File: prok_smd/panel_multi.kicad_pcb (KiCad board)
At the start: 2 copper layers, 80 x 128.5 mm, 4 parts

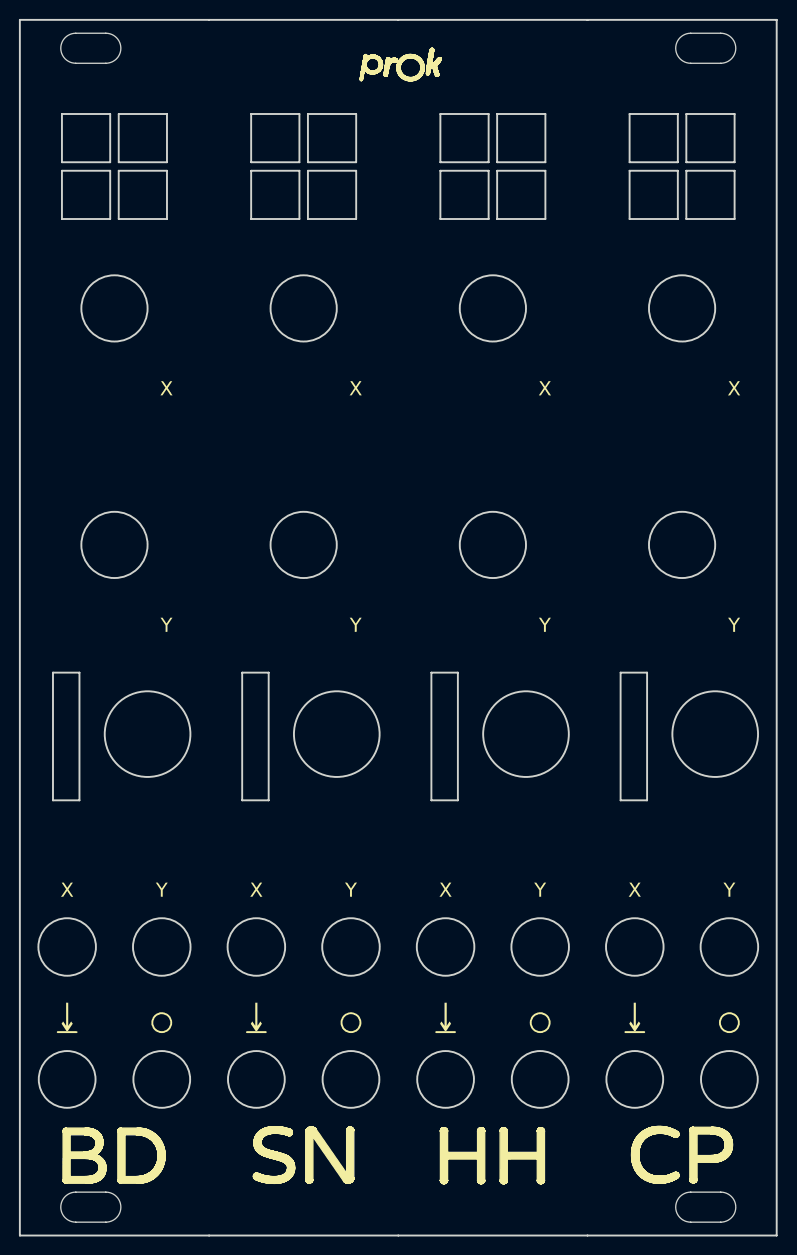
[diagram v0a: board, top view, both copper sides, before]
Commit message: :lipstick: Panel (x4) changed graphics (plaits style) & changed name ;)
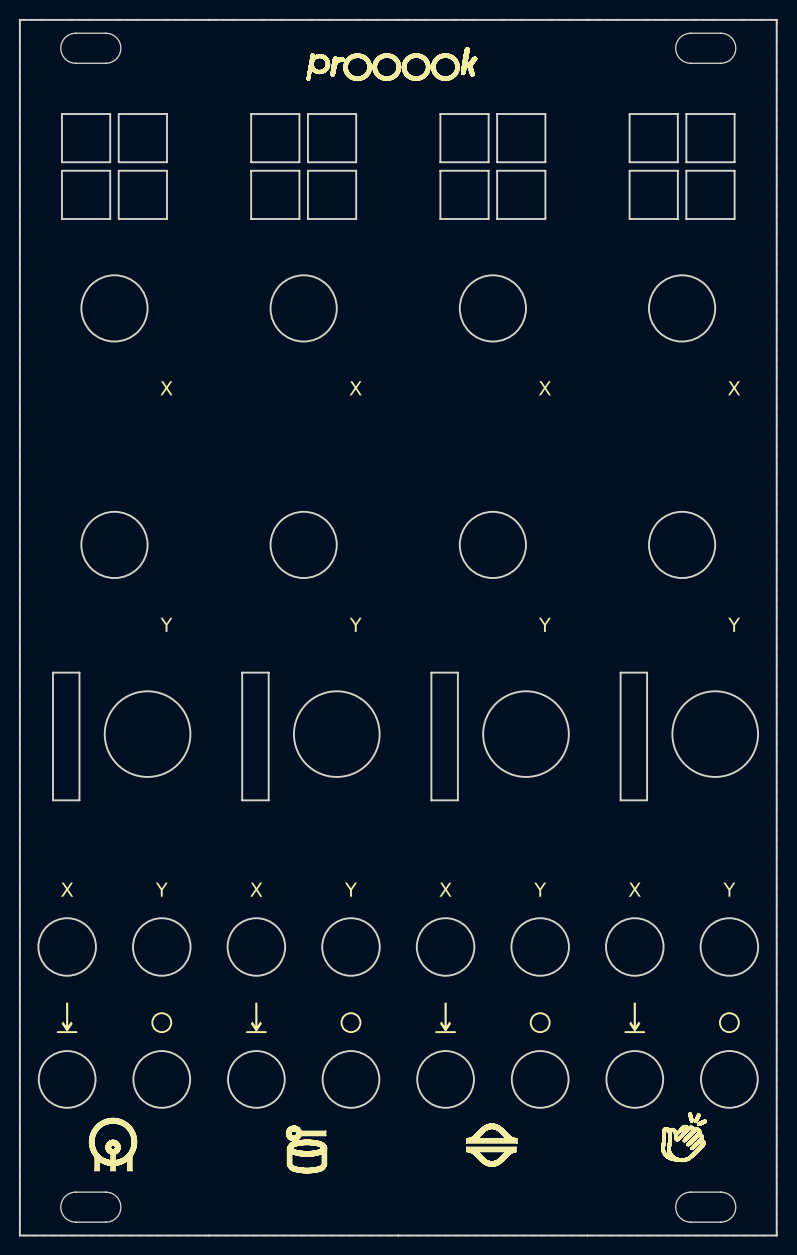
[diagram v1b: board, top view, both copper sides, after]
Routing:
- added copper zone on B.Cu, net (none)
- added copper zone on F.Cu, net (none)

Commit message: :lipstick: :sparkles: Gold (soldermask hole) instead of silkscreen
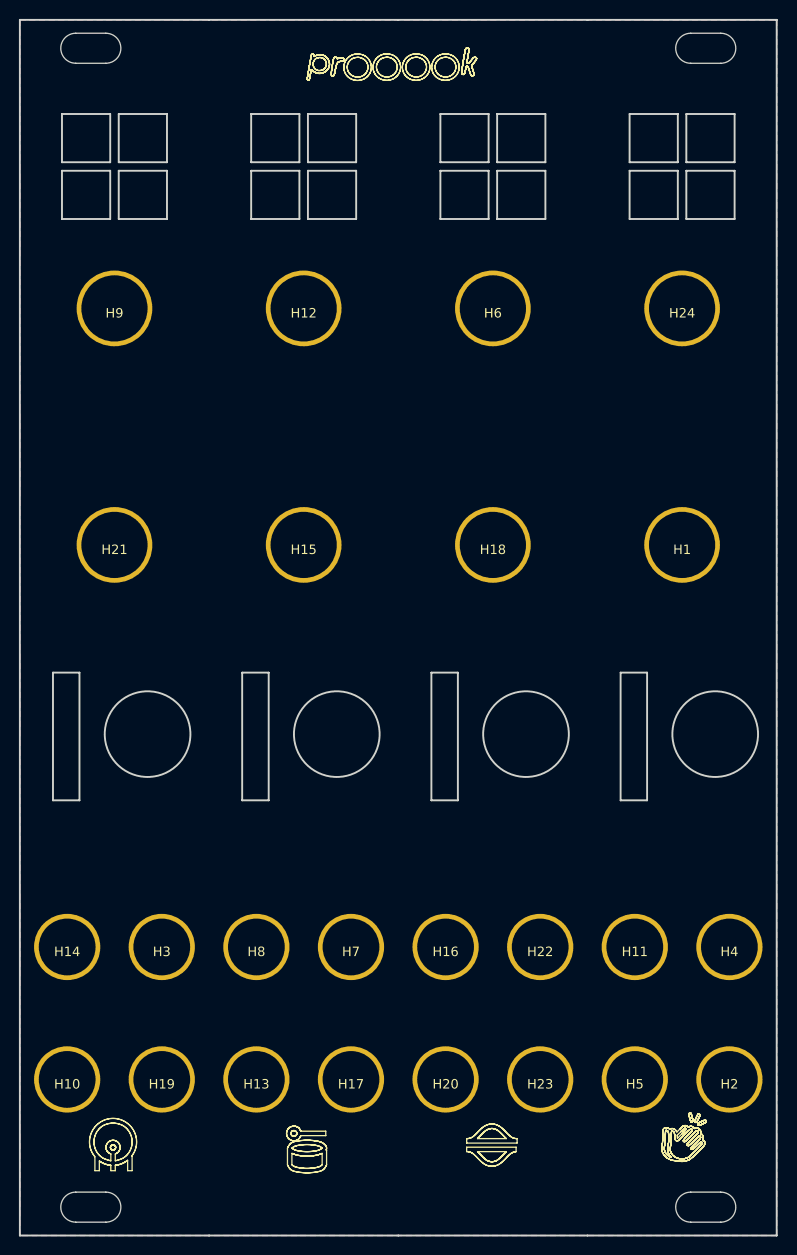
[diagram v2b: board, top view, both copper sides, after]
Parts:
- added H1: MountingHole_Pad, prok_smd:Alpha_pot_hole_metallized, F.Cu at (120.0, 105.5)
- added H10: MountingHole_Pad, prok_smd:thonkiconn_hole_metallized, F.Cu at (55.0, 162.0)
- added H11: MountingHole_Pad, prok_smd:thonkiconn_hole_metallized, F.Cu at (115.0, 148.0)
- added H12: MountingHole_Pad, prok_smd:Alpha_pot_hole_metallized, F.Cu at (80.0, 80.5)
- added H13: MountingHole_Pad, prok_smd:thonkiconn_hole_metallized, F.Cu at (75.0, 162.0)
- added H14: MountingHole_Pad, prok_smd:thonkiconn_hole_metallized, F.Cu at (55.0, 148.0)
- added H15: MountingHole_Pad, prok_smd:Alpha_pot_hole_metallized, F.Cu at (80.0, 105.5)
- added H16: MountingHole_Pad, prok_smd:thonkiconn_hole_metallized, F.Cu at (95.0, 148.0)
- added H17: MountingHole_Pad, prok_smd:thonkiconn_hole_metallized, F.Cu at (85.0, 162.0)
- added H18: MountingHole_Pad, prok_smd:Alpha_pot_hole_metallized, F.Cu at (100.0, 105.5)
- added H19: MountingHole_Pad, prok_smd:thonkiconn_hole_metallized, F.Cu at (65.0, 162.0)
- added H2: MountingHole_Pad, prok_smd:thonkiconn_hole_metallized, F.Cu at (125.0, 162.0)
- added H20: MountingHole_Pad, prok_smd:thonkiconn_hole_metallized, F.Cu at (95.0, 162.0)
- added H21: MountingHole_Pad, prok_smd:Alpha_pot_hole_metallized, F.Cu at (60.0, 105.5)
- added H22: MountingHole_Pad, prok_smd:thonkiconn_hole_metallized, F.Cu at (105.0, 148.0)
- added H23: MountingHole_Pad, prok_smd:thonkiconn_hole_metallized, F.Cu at (105.0, 162.0)
- added H24: MountingHole_Pad, prok_smd:Alpha_pot_hole_metallized, F.Cu at (120.0, 80.5)
- added H3: MountingHole_Pad, prok_smd:thonkiconn_hole_metallized, F.Cu at (65.0, 148.0)
- added H4: MountingHole_Pad, prok_smd:thonkiconn_hole_metallized, F.Cu at (125.0, 148.0)
- added H5: MountingHole_Pad, prok_smd:thonkiconn_hole_metallized, F.Cu at (115.0, 162.0)
- added H6: MountingHole_Pad, prok_smd:Alpha_pot_hole_metallized, F.Cu at (100.0, 80.5)
- added H7: MountingHole_Pad, prok_smd:thonkiconn_hole_metallized, F.Cu at (85.0, 148.0)
- added H8: MountingHole_Pad, prok_smd:thonkiconn_hole_metallized, F.Cu at (75.0, 148.0)
- added H9: MountingHole_Pad, prok_smd:Alpha_pot_hole_metallized, F.Cu at (60.0, 80.5)
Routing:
- added copper zone on B.Cu, net GND
- added copper zone on F.Cu, net GND
- removed copper zone on B.Cu, net (none)
- removed copper zone on F.Cu, net (none)
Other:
- outline, holes or cut-outs redrawn
